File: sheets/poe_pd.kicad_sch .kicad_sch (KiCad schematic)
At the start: 0 parts

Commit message: pwr section design
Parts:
- added C1, C2, C3, C4: 1n, symbol Device:C
- added J1: 0826-1X1T-HS-F, 0826-1X1T-HS-F:BEL_0826-1X1T-HS-F, symbol poe-aes67-amp:0826-1X1T-HS-F
- added R1, R2: 68R, symbol Device:R
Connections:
- new net: C2.1, J1.14 (VC2)
- new net: C1.1, J1.13 (VC1)
- new net: C3.1, J1.15 (VC3)
- new net: C4.1, J1.16 (VC4)
- new net: J1.17, R1.1
- new net: J1.19, R2.1
- new net +3.3V: R1.2, R2.2
- new net GND: C1.2, C2.2, C3.2, C4.2, J1.18
- new net GNDPWR: J1.SH1 (SHIELD), J1.SH2 (SHIELD__1)
- new net LED_ACT: J1.20

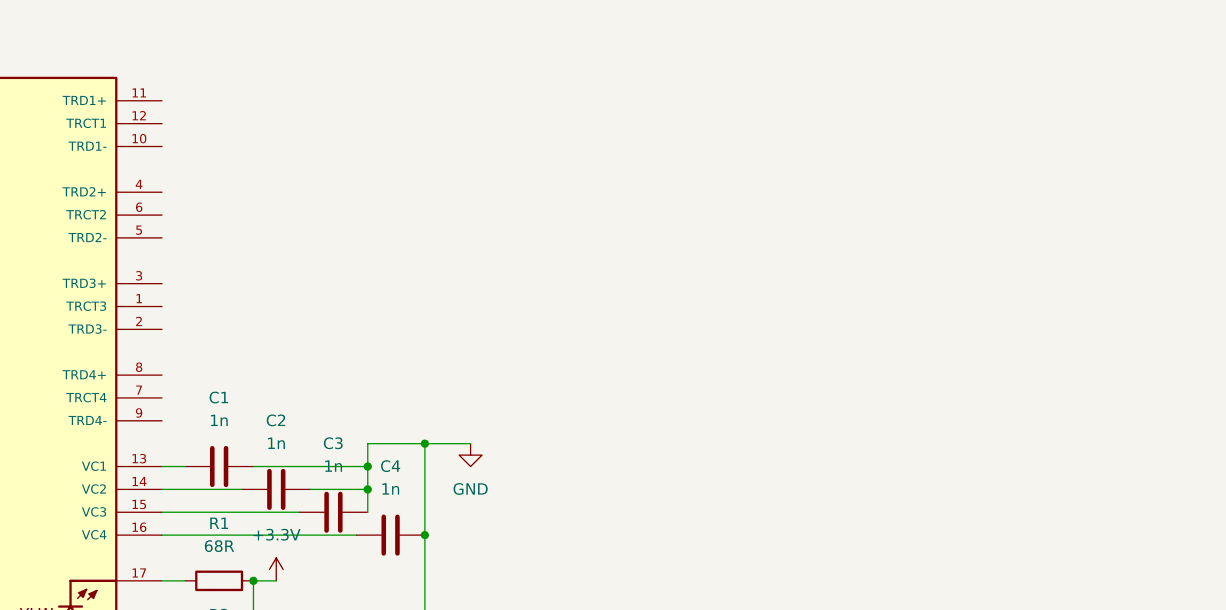
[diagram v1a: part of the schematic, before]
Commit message: Add MagJack, bridge rectifier, and VPOE filtering - Sheet 2
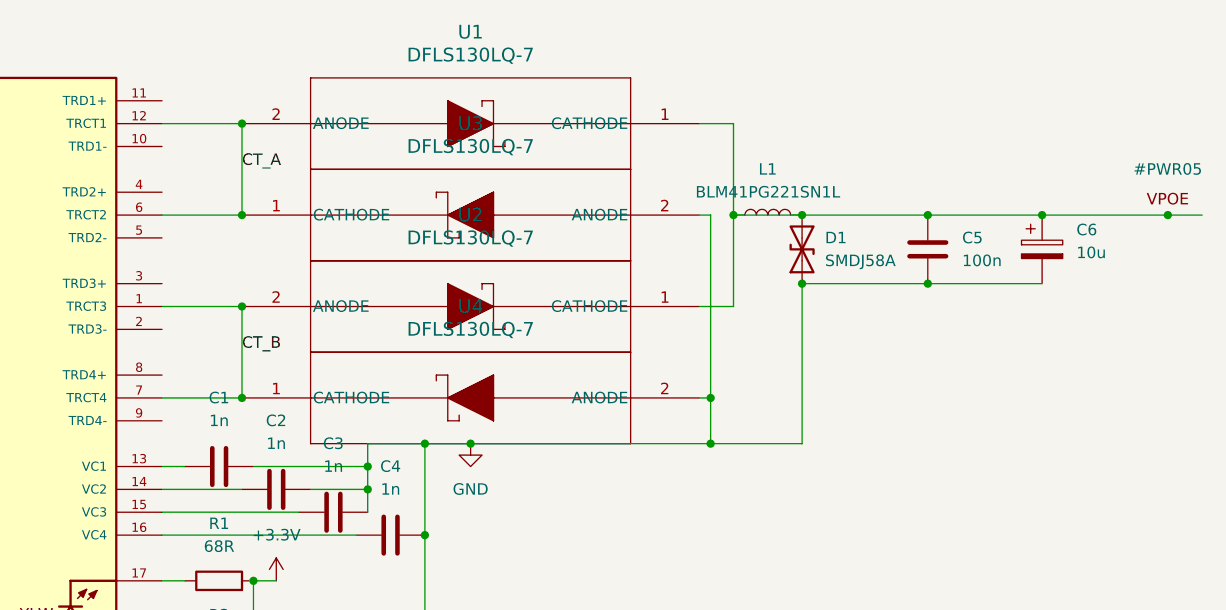
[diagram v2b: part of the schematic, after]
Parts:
- added C5: 100n, symbol Device:C
- added C6: 10u, symbol Device:C_Polarized
- added D1: SMDJ58A, symbol Device:D_TVS
- added L1: BLM41PG221SN1L, symbol Device:L
- added U1, U2, U3, U4: DFLS130LQ-7, DFLS130-7_DIO, symbol poe-aes67-amp:DFLS130LQ-7
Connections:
- net GND: now also C5.2, C6.2, D1.1 (A1), U3.2 (ANODE), U4.2 (ANODE)
- net CT_B: now reaches J1.1 (TRCT3)
- net CT_B: now also J1.7 (TRCT4), U2.2 (ANODE), U4.1 (CATHODE)
- net CT_A: now reaches J1.12 (TRCT1)
- net CT_A: now also J1.6 (TRCT2), U1.2 (ANODE), U3.1 (CATHODE)
- new net: C5.1, C6.1, D1.2 (A2), L1.1, L1.2, U1.1 (CATHODE), U2.1 (CATHODE)

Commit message: Complete Sheet 2 - PoE PD section
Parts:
- added C7, C8: 100n, symbol Device:C
- added C9: 220u, symbol Device:C_Polarized
- added R10, R11, R12, R6, R7, R8, R9: 100k, symbol Device:R
- added R3: 24.9k, symbol Device:R
- added R4: 619, symbol Device:R
- added R5: 1k, symbol Device:R
- added U5: TPS2372-4RGWR, RGW0020B, symbol poe-aes67-amp:TPS2372-4RGWR
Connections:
- net GND: now also C7.1, C8.2, C9.2, R11.2, R4.1, R5.1, R7.1, R8.1, U5.11 (RTN), U5.12 (RTN), U5.21 (VSS), U5.4 (VSS), U5.5 (VSS)
- net MDI1_N: now reaches J1.10 (TRD1-)
- net MDI1_P: now reaches J1.11 (TRD1+)
- net MDI3_N: now reaches J1.2 (TRD3-)
- net MDI3_P: now reaches J1.3 (TRD3+)
- net MDI2_P: now reaches J1.4 (TRD2+)
- net MDI2_N: now reaches J1.5 (TRD2-)
- net MDI4_P: now reaches J1.8 (TRD4+)
- net MDI4_N: now reaches J1.9 (TRD4-)
- new net: R11.1, U5.17 (TPL)
- new net: R5.2, U5.6 (CLSB)
- new net: C8.1, U5.19 (BT_N)
- new net: C7.2, U5.7 (REF)
- new net: R8.2, U5.9 (MPS_DUTY)
- new net: R6.2, U5.10 (AUTCLS_N)
- new net: R10.1, U5.18 (TPH)
- new net: C9.1, R10.2, R12.2, R9.2
- new net: R3.2, U5.2 (DEN)
- new net: R12.1, U5.16 (IRSHDL_EN)
- new net: R4.2, U5.3 (CLSA)
- new net: R7.2, U5.8 (AMPS_CTL)
- new net BUCK_A_EN: R9.1, U5.13 (PG)
- no-connect marks 0 -> 3

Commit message: Complete Sheet 2 - PoE PD section
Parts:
- added R13: 0, symbol Device:R
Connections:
- net GND: now also R13.2
- net GNDPWR: now also R13.1
- net at R6.1: now also R3.1, U5.1 (VDD)
